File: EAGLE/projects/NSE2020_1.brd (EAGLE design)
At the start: 80 x 80 mm, 48 parts, among them CN1 MICROSD, IC1 ADP3338-3.3, X1 MINI-USB-UX60A-MB-5ST

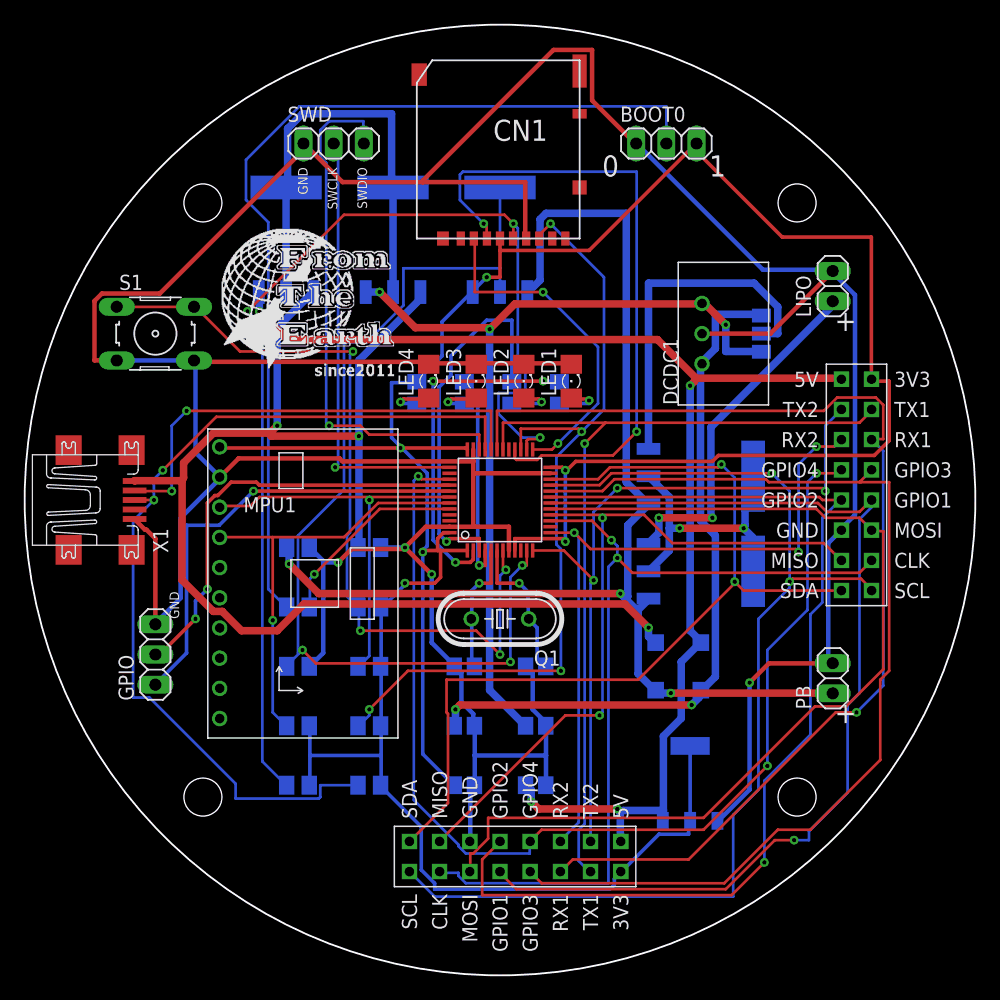
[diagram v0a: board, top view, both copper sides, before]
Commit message: 第2次試作で見つかったミスの修正
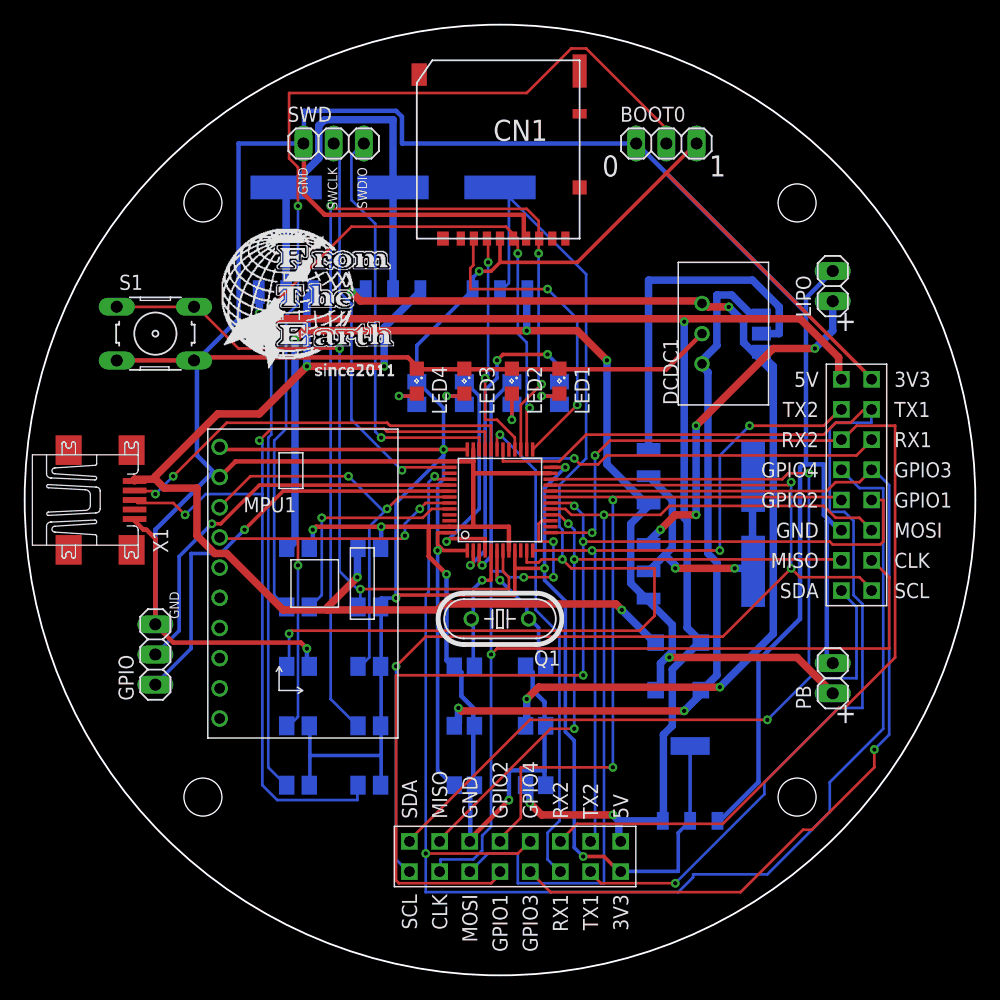
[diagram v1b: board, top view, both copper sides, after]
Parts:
- LED1, LED2, LED3, LED4: device led:1206 -> led:SML0805
- moved LED1 1.00 mm to (45.0, 50.0), turned to 270 degrees
- moved LED2 1.00 mm to (41.0, 50.0), turned to 270 degrees
- moved LED3 1.00 mm to (37.0, 50.0), turned to 270 degrees
- moved LED4 1.00 mm to (33.0, 50.0), turned to 270 degrees
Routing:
- net MOSI2: track 55.4 -> 19.6 mm
- net RX_2: track 60.1 -> 90.6 mm, vias 3 -> 2
- net GND: track 358.2 -> 384.4 mm, vias 4 -> 5
- net GPIO2: track 87.9 -> 62.0 mm, vias 1 -> 2
- net RX_1: track 95.1 -> 71.6 mm, vias 1 -> 2
- net GPIO4: track 94.0 -> 116.1 mm, vias 3 -> 2
- net TX_1: track 73.0 -> 94.1 mm
- net +3V3: track 256.2 -> 236.6 mm, vias 6 -> 7
- net DCDC2FET: track 73.1 -> 90.0 mm, vias 3 -> 4
- net V+: track 111.4 -> 96.2 mm, vias 3 -> 4
- net MISO2: track 69.3 -> 82.9 mm, vias 4 -> 3
- net IO2R2: track 31.7 -> 18.1 mm
- net SDA2: track 77.3 -> 90.6 mm
- net PBDET: track 84.3 -> 95.2 mm, vias 3 -> 2
- net SCK1: track 72.3 -> 82.8 mm, vias 2 -> 4
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
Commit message: 第3次試作修正(USB抵抗、BOOT1プルダウン)
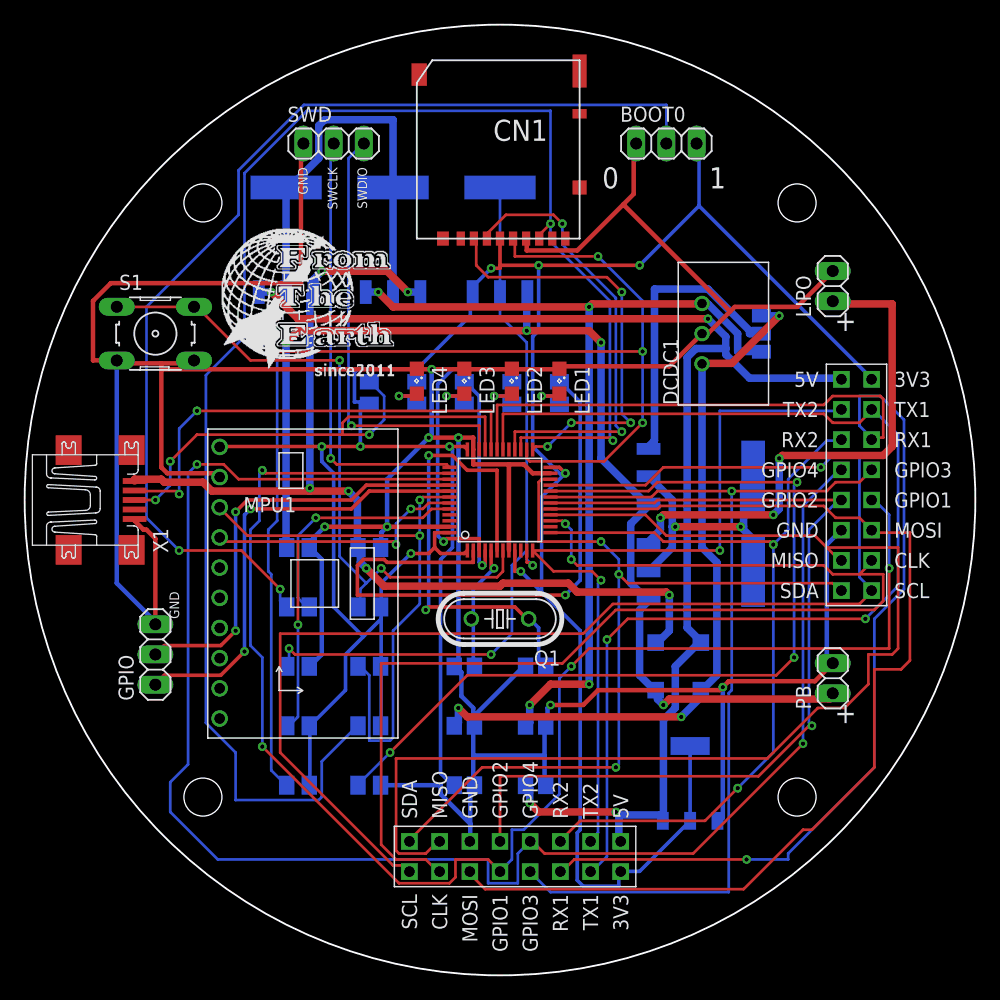
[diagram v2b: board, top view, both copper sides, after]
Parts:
- added R15: 1k, rcl:M2012
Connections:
- new net BOOT1: MCU1.20, R10.1
- net +3V3: now also R15.2; no longer R10.2
- net DP: now also R15.1; no longer R10.1
- net GND: now also R10.2
- net GPIO1: now also MCU1.38; no longer MCU1.18
- net GPIO2: now also MCU1.18; no longer MCU1.19
- net GPIO3: now also MCU1.19; no longer MCU1.20
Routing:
- net BOOT1: track 0.00 -> 77.2 mm, vias 0 -> 3
- net MISO2: track 82.9 -> 138.2 mm, vias 3 -> 2
- net MISO1: track 57.1 -> 100.0 mm, vias 3 -> 0
- net GPIO1: track 89.0 -> 127.8 mm, vias 3 -> 4
- net RX_1: track 71.6 -> 110.2 mm, vias 2 -> 1
- net PBDET: track 95.2 -> 63.4 mm, vias 2 -> 3
- net GND: track 384.4 -> 354.3 mm, vias 5 -> 7
- net OSC_OUT: track 11.8 -> 40.0 mm, vias 1 -> 2
- net DP: track 71.9 -> 44.7 mm, vias 2 -> 3
- net +3V3: track 236.6 -> 262.9 mm, vias 7 -> 9
- net SCL2: track 89.7 -> 115.2 mm, vias 3 -> 1
- net GPIO4: track 116.1 -> 140.5 mm
- net IO2R1: track 26.9 -> 50.4 mm, vias 3 -> 1
- net RX_2: track 90.6 -> 69.6 mm
- net SCK2: track 83.8 -> 104.7 mm, vias 3 -> 4
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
